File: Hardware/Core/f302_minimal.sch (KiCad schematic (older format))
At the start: 43 parts, among them J1 USB_B_Micro, J2 Conn_02x10_Odd_Even, J3 Conn_02x10_Odd_Even, J4 Conn_01x04, SW1 SW_Push, U1 USBLC6-2SC6, U2 AMS1117-3.3, U3 LP5907MFX-3.3, U4 QMI8658C, U5 STM32F302C8Tx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

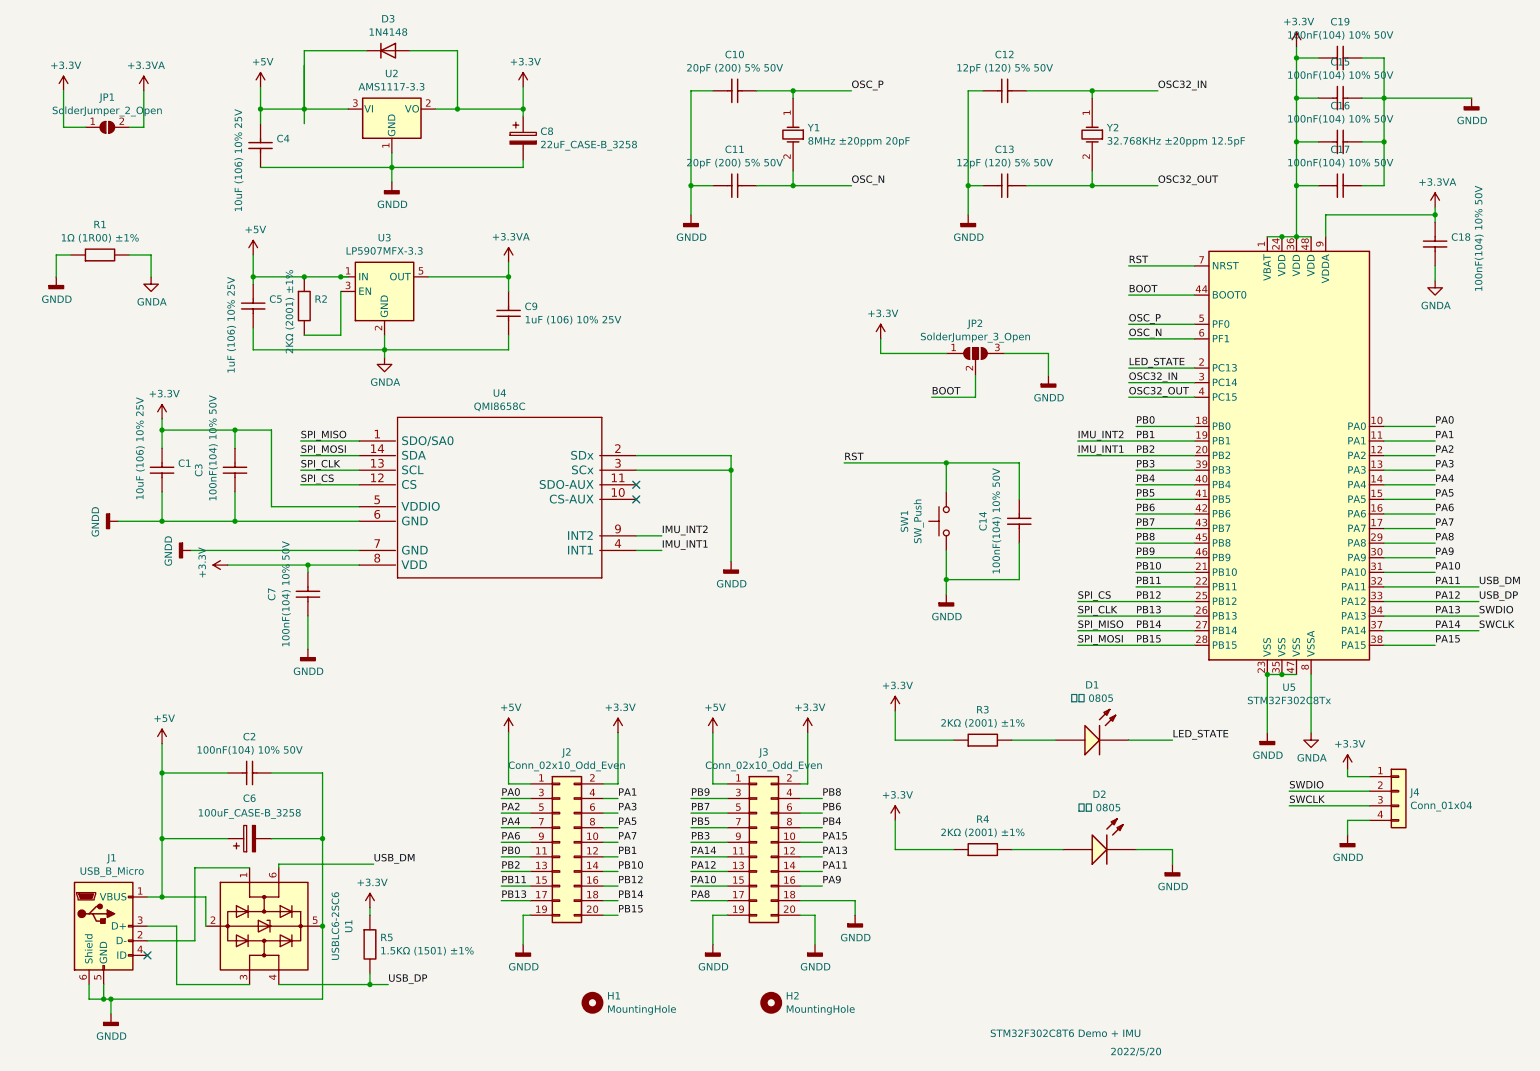
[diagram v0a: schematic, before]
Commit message: update hardware, add eskf code, bug fix
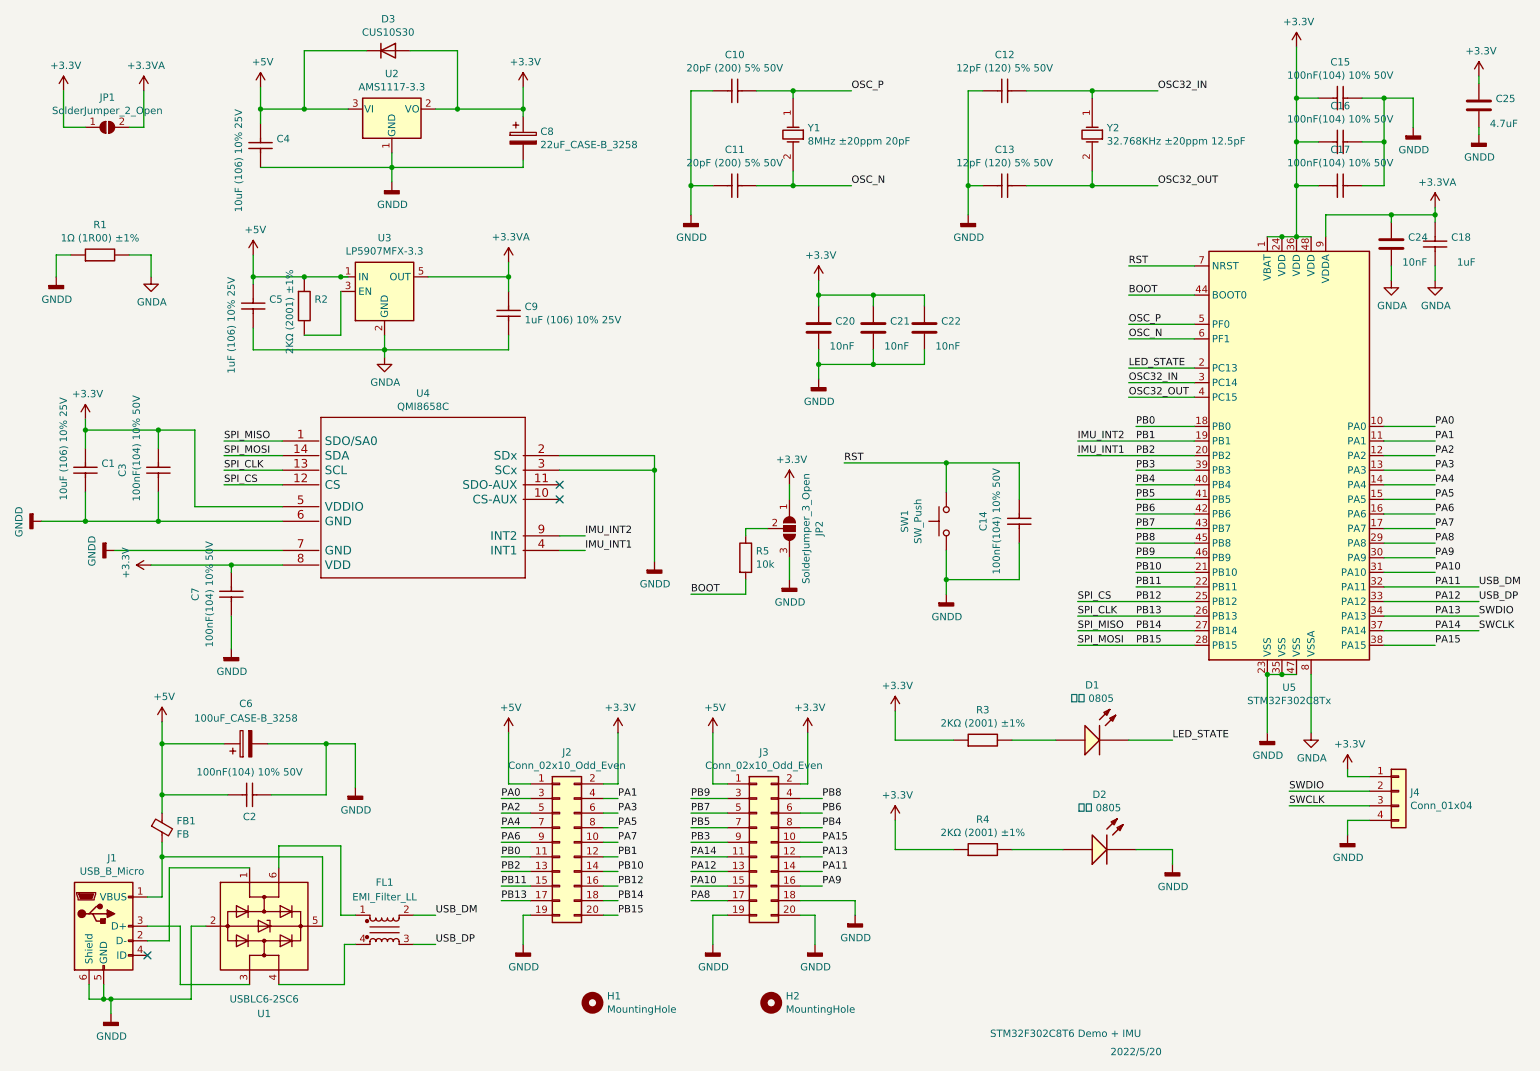
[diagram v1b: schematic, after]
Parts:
- removed C19: 0805_100nF_104_10%_50V, lc_lib:0805_C, symbol lc_Cap:0805_100nF_104_10%_50V
- removed R5: 0805_1.5KΩ__1501_1%, lc_lib:0805_R, symbol lc_RES:0805_1.5KΩ__1501_1%
- added C20, C21, C22, C24: 10nF, Capacitor_SMD:C_0603_1608Metric_Pad1.08x0.95mm_HandSolder, symbol Device:C
- added C25: 4.7uF, Capacitor_SMD:C_0805_2012Metric_Pad1.18x1.45mm_HandSolder, symbol Device:C
- added FB1: FB, Resistor_SMD:R_0805_2012Metric_Pad1.20x1.40mm_HandSolder, symbol Device:Ferrite_Bead_Small
- added FL1: EMI_Filter_LL, Core:DLW21SN900SQ2L, symbol EMI_FILTER:EMI_Filter_LL
- added R5: 10k, Resistor_SMD:R_0603_1608Metric_Pad0.98x0.95mm_HandSolder, symbol Device:R
- C12, C13: footprint lc_lib:0805_C -> lc_lib:0603_C
- C18: value 0805_100nF_104_10%_50V -> 1uF; Comment 100nF(104) 10% 50V -> 1uF
- D3: value 1N4148 -> CUS10S30; footprint Diode_SMD:D_MiniMELF_Handsoldering -> Diode_SMD:D_SOD-323_HandSoldering
- U1: footprint Package_TO_SOT_SMD:SOT-23-6 -> Package_TO_SOT_SMD:SOT-23-6_Handsoldering
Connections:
- net +3.3VA: now also C24.1
- net +3V3: now also C20.1, C21.1, C22.1, C25.1
- net +5V: now also FB1.1; no longer J1.1 (VBUS), U1.2 (GND)
- net BOOT: now also R5.2; no longer JP2.2 (C)
- net GNDA: now also C24.2
- net GNDD: now also U1.2 (GND), C20.2, C21.2, C22.2, C25.2; no longer U1.5 (VBUS)
- net PA11: now also FL1.2; no longer U1.6 (I/O1)
- net PA12: now also FL1.3; no longer U1.4 (I/O2)
- new net: FL1.4, U1.4 (I/O2)
- new net: FB1.2, J1.1 (VBUS), U1.5 (VBUS)
- new net: FL1.1, U1.6 (I/O1)
- new net: JP2.2 (C), R5.1
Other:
- moved on the sheet: C1, C2, C3, C6, C7, JP2, U4
